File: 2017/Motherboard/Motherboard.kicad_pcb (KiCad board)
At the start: 2 copper layers, 47 parts, among them P1 DB9, P2 PROGRAM+DEBUG, P3 PCIe Card 1, P4 PCIe Card 2, P5 PCIe Card 3, SW1 SPST, U1 MSP432, U2 LM340MP-5.0, U3 LD1086DT33TR, U4 MCP9808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

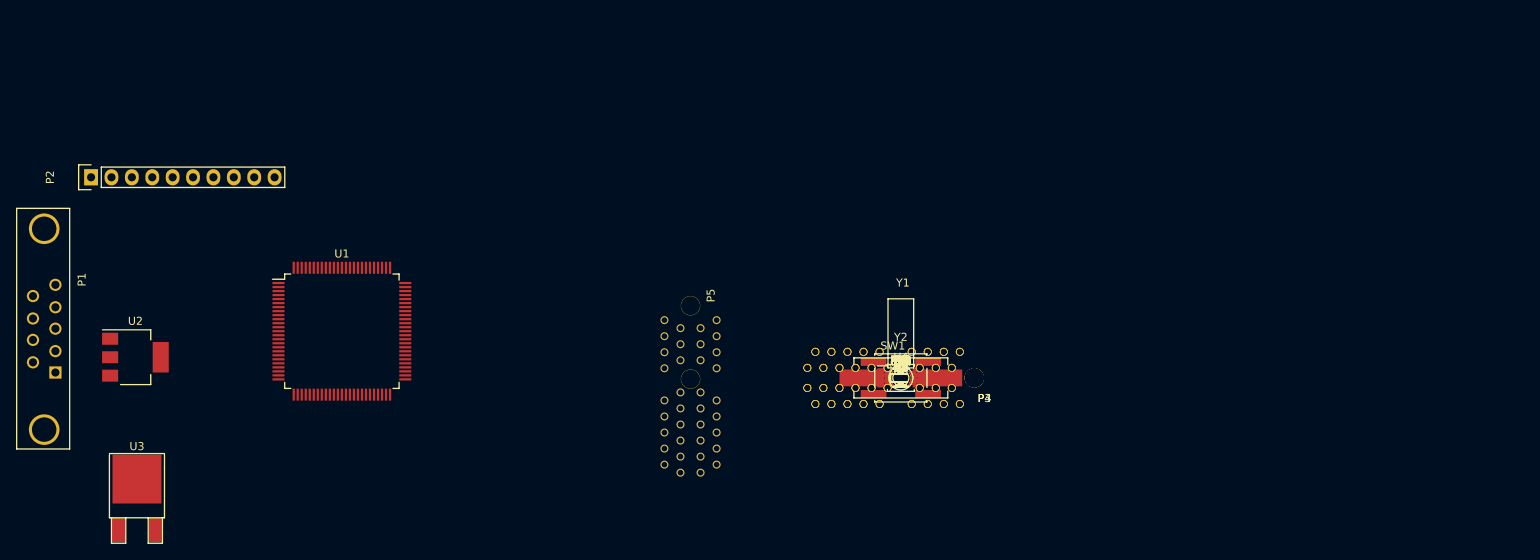
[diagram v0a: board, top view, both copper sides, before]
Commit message: Finish Mobo v1.0
Add XT60 power conector, add mounting holes, finish layout of
Motherboard v1.0
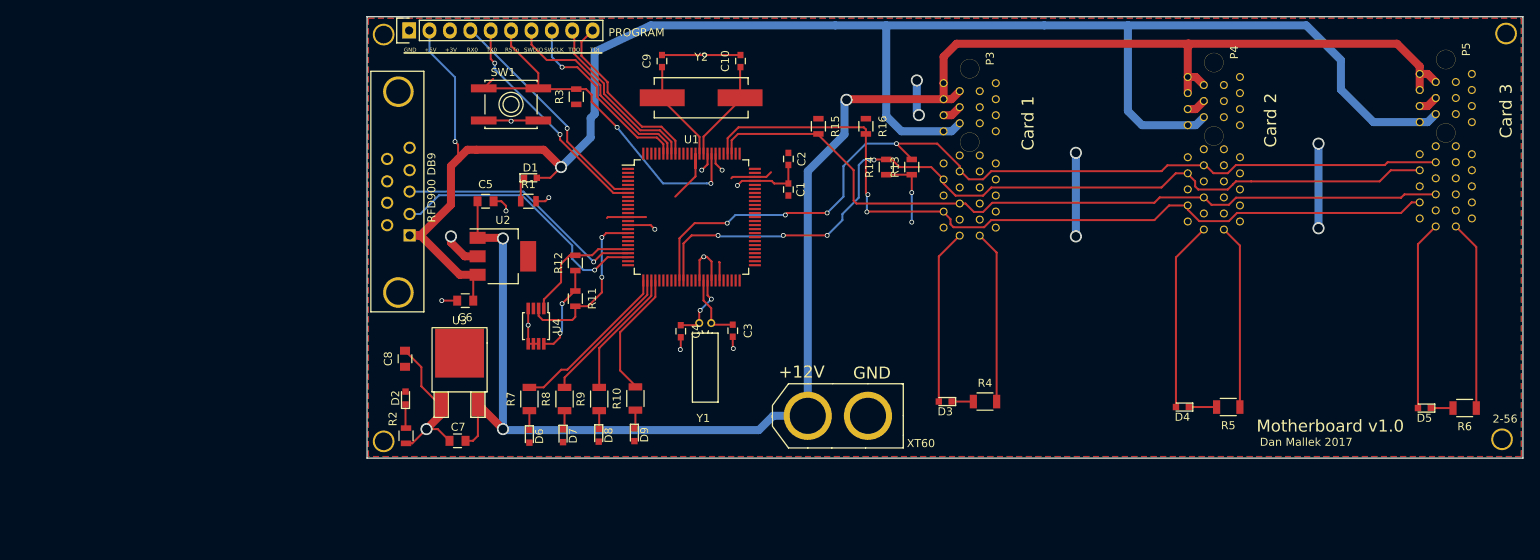
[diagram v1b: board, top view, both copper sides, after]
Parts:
- added 2-56: 2-56 Standoff, Mounting_Holes:2-56_Standoff, F.Cu at (224.2, 108.6)
- added 2-56: 2-56 Standoff, Mounting_Holes:2-56_Standoff, F.Cu at (224.7, 58.0)
- added 2-56: 2-56 Standoff, Mounting_Holes:2-56_Standoff, F.Cu at (84.8, 108.8)
- added 2-56: 2-56 Standoff, Mounting_Holes:2-56_Standoff, F.Cu at (84.8, 58.2)
- added G***: LOGO, MAVRIC_Logo:MAVRIC_Logo, B.Cu at (160.0, 92.0)
- added XT60: 12v POWER, XT60:XT60, F.Cu at (136.9, 109.7)
- RFD900 DB9: renamed from P1
- moved P5 99.0 mm to (216.4, 74.5)
- moved R6 70.3 mm to (218.7, 108.8), turned to 180 degrees
- moved D5 65.3 mm to (213.7, 108.8), turned to 180 degrees
- moved R2 62.1 mm to (86.9, 112.2), turned to 90 degrees
- moved C8 61.8 mm to (86.7, 102.6), turned to 90 degrees
- moved D2 61.8 mm to (86.8, 107.5), turned to 90 degrees
- moved SW1 59.3 mm to (99.9, 70.9)
- moved C5 56.2 mm to (96.8, 83.0)
- moved C7 55.8 mm to (93.3, 112.8), turned to 180 degrees
- moved C6 55.1 mm to (94.2, 95.4), turned to 180 degrees
- moved R3 53.5 mm to (108.1, 70.0), turned to 90 degrees
- moved D1 52.5 mm to (102.4, 80.1)
- moved R1 51.4 mm to (102.1, 83.0)
- moved C9 49.4 mm to (118.7, 65.5), turned to 90 degrees
- moved P4 49.3 mm to (187.5, 74.9), turned to 90 degrees
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- renumbered P2 to PROGRAM
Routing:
- net +5V: track 0.00 -> 234.1 mm, vias 0 -> 2
- net +12V: track 0.00 -> 217.2 mm, vias 0 -> 3
- net /SDA0: track 0.00 -> 113.3 mm, vias 0 -> 4
- net /SCL0: track 0.00 -> 109.2 mm, vias 0 -> 4
- net /SCL1: track 0.00 -> 103.6 mm, vias 0 -> 2
- net /SDA1: track 0.00 -> 97.7 mm
- net GND: track 0.00 -> 79.9 mm, vias 0 -> 15
- net +3V3: track 0.00 -> 48.5 mm, vias 0 -> 4
- net /RSTn: track 0.00 -> 48.2 mm, vias 0 -> 2
- net /RX1: track 0.00 -> 33.7 mm, vias 0 -> 1
- net /TX1: track 0.00 -> 31.3 mm, vias 0 -> 1
- net /UCA0RXD: track 0.00 -> 28.9 mm, vias 0 -> 1
- net /UCA0TXD: track 0.00 -> 28.6 mm, vias 0 -> 2
- net /SWDIO: track 0.00 -> 25.9 mm
- net (no net): track 0.00 -> 25.5 mm, vias 0 -> 6
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- added copper zone on F.Cu, net +3V3
- added copper zone on B.Cu, net GND
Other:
- board outline added: 144 x 55 mm
- board text added: "+12V"
- board text added: "+3V"
- board text added: "+5V"
- board text added: "Card 1"
- board text added: "Card 2"
- board text added: "Card 3"
- board text added: "Dan Mallek 2017"
- board text added: "GND"
- board text added: "Motherboard v1.0"
- board text added: "RSTn"
- board text added: "RX0"
- board text added: "SWCLK"
- board text added: "SWDIO"
- board text added: "TDI"
- board text added: "TDO"
- board text added: "TX0"
